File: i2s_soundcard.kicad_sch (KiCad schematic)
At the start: 19 parts, among them J1 Conn_01x08, J2 Conn_01x06, J3 Conn_01x04, J4 Conn_01x11, J5 Conn_01x03, U1 TLV320AIC3104IRHBT, U6 TLV7111830DSER, U7 TPD4E02B04DQAR, U8 TPD4E02B04DQAR

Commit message: Schematic: switch to AIC3206 to get ground-centered headphone outputs, and just wire up directly to a raspberry pi 40-pin header instead of using 1mm headers.
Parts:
- removed C2, C3: 220uF, Capacitor_SMD:C_1206_3216Metric, symbol Device:C
- removed C5: 22uF, Capacitor_SMD:C_0402_1005Metric, symbol Device:C
- removed C9: 220nF, Capacitor_SMD:C_0402_1005Metric, symbol Device:C
- removed J3: Conn_01x04, Connector_PinHeader_1.00mm:PinHeader_1x04_P1.00mm_Vertical, symbol Connector_Generic:Conn_01x04
- removed J4: Conn_01x11, Connector_PinHeader_1.00mm:PinHeader_1x11_P1.00mm_Vertical, symbol Connector_Generic:Conn_01x11
- removed U1: TLV320AIC3104IRHBT, footprints:TLV320AIC3104IRHBT, symbol TLV320AIC3104IRHBT:TLV320AIC3104IRHBT
- added C? (x2): 2.2uF, symbol Device:C
- added C? (x2): 10uF, Capacitor_SMD:C_0402_1005Metric, symbol Device:C
- added C?: 0.1uF, Capacitor_SMD:C_0402_1005Metric, symbol Device:C
- added C? (x2): 0.1u, symbol Device:C
- added C?: 1uF, symbol Device:C
- added J?: Conn_02x20_Odd_Even, symbol Connector_Generic:Conn_02x20_Odd_Even
- added R? (x2): 1k, symbol Device:R
- added U?: TLV320AIC3206IRSBR, RSB0040B, symbol TLV320AIC3206IRSBR:TLV320AIC3206IRSBR
- R1: value 2.2k -> 2.7k
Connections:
- net BCLK: now also J?.12 (Pin_12), U?.6 (BCLK)
- net DIN: now also J?.40 (Pin_40), U?.8 (DIN_MFP1)
- net DOUT: now also J?.38 (Pin_38), U?.9 (DOUT_MFP2)
- net GND: now also C?.1, C?.1, C?.1, C?.2, C?.2, J?.14 (Pin_14), J?.20 (Pin_20), J?.25 (Pin_25), J?.30 (Pin_30), J?.34 (Pin_34), J?.39 (Pin_39), J?.6 (Pin_6), J?.9 (Pin_9), R?.2, U?.1 (DVSS), U?.11 (IOVSS), U?.16 (SPI_SELECT), U?.2 (DVSS), U?.21 (AVSS), U?.37 (DVSS_CP), U?.41 (PAD); no longer J1.4 (Pin_4)
- net INTMIC_N: now also C?.2
- net INTMIC_P: now also C?.2
- net IOVDD: now also J?.1 (Pin_1), J?.17 (Pin_17), U?.10 (IOVDD)
- net LOL: now also U?.26 (LOL)
- net LOR: now also U?.27 (LOR)
- net MCLK: now also U?.5 (MCLK)
- net RING1: now also U?.33 (HPR)
- net SCL: now also J?.5 (Pin_5), U?.13 (SCL_SS_N)
- net SLEEVE: now also R1.2, U?.34 (MICDET); no longer R1.1
- net TIP: now also U?.31 (HPL)
- net VCC1.8: now also C?.2, C?.2, U?.29 (AVDD), U?.32 (DRVDD_HP), U?.39 (DVDD_CP), U?.40 (DVDD); no longer U6.6 (OUT1)
- net WCLK: now also J?.35 (Pin_35), U?.7 (WCLK)
- net at C1.1: now also U?.24 (IN3_L)
- net RING2: now reaches U7.5 (D2-)
- net RING2: now also J1.4 (Pin_4), U7.6 (NC), U?.28 (GND_SENSE)
- net EN1 renamed LDO_EN1
- net LDO_EN1: now also J?.15 (Pin_15)
- net EN2: no longer names the net of U6.3 (EN2)
- net VBAT_3.7 renamed VSYS
- net VSYS: now also C?.2, J?.2 (Pin_2), J?.4 (Pin_4), U?.30 (VSYS)
- net VCC3.0: no longer names the net of U6.5 (OUT2)
- new net: R1.1, R?.2, U?.23 (MICBIAS)
- new net: C?.1, U?.36 (FLY_N)
- new net: C?.2, U?.38 (FLY_P)
- new net: C?.1, R?.1, U?.18 (IN1_R)
- new net: C?.1, R?.1, U?.17 (IN1_L)
- new net: C?.1, U?.35 (VNEG)
- new net: C?.1, U?.22 (REF)
- new net CODEC_RESET: J?.13 (Pin_13), U?.3 (RESET_N)
- new net SDA: J?.3 (Pin_3), U?.14 (SDA_MOSI)
- new net ~AMP_SHUTDOWN: J?.11 (Pin_11)
- no-connect marks 4 -> 27
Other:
- sheet spkr_amp_left ports: added LINEIN; removed LINEIN+, LINEIN-
- sheet spkr_amp_right ports: added LINEIN; removed LINEIN+, LINEIN-
- moved on the sheet: C1, C10, C11, C4, C8, J1, R1, U7, U8

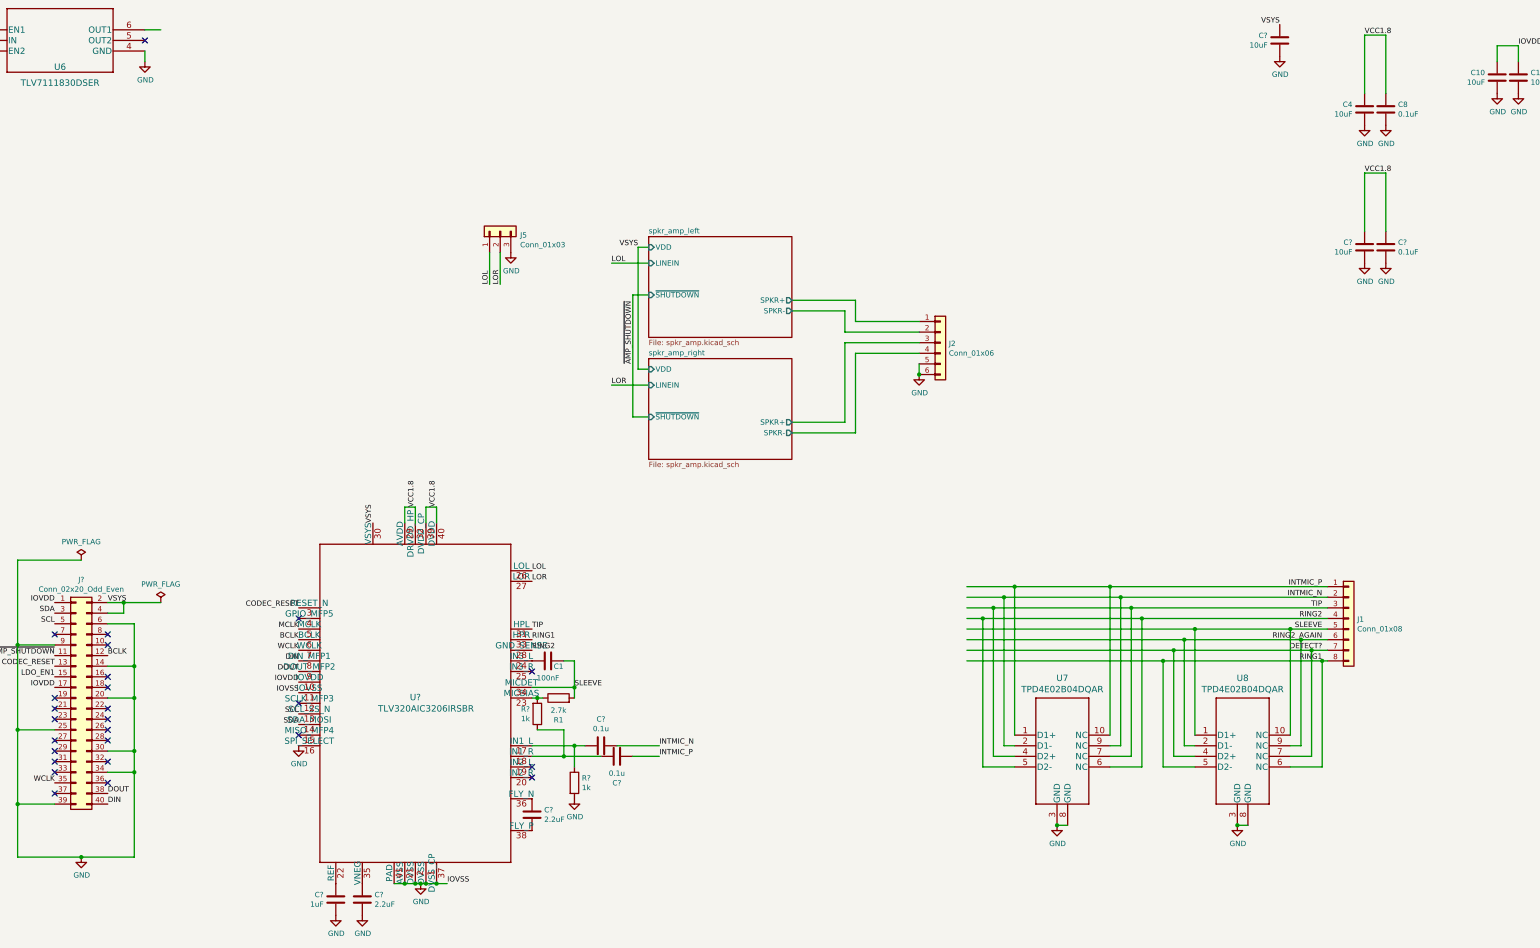
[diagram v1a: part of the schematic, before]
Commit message: lay out new version with AIC3206 codec
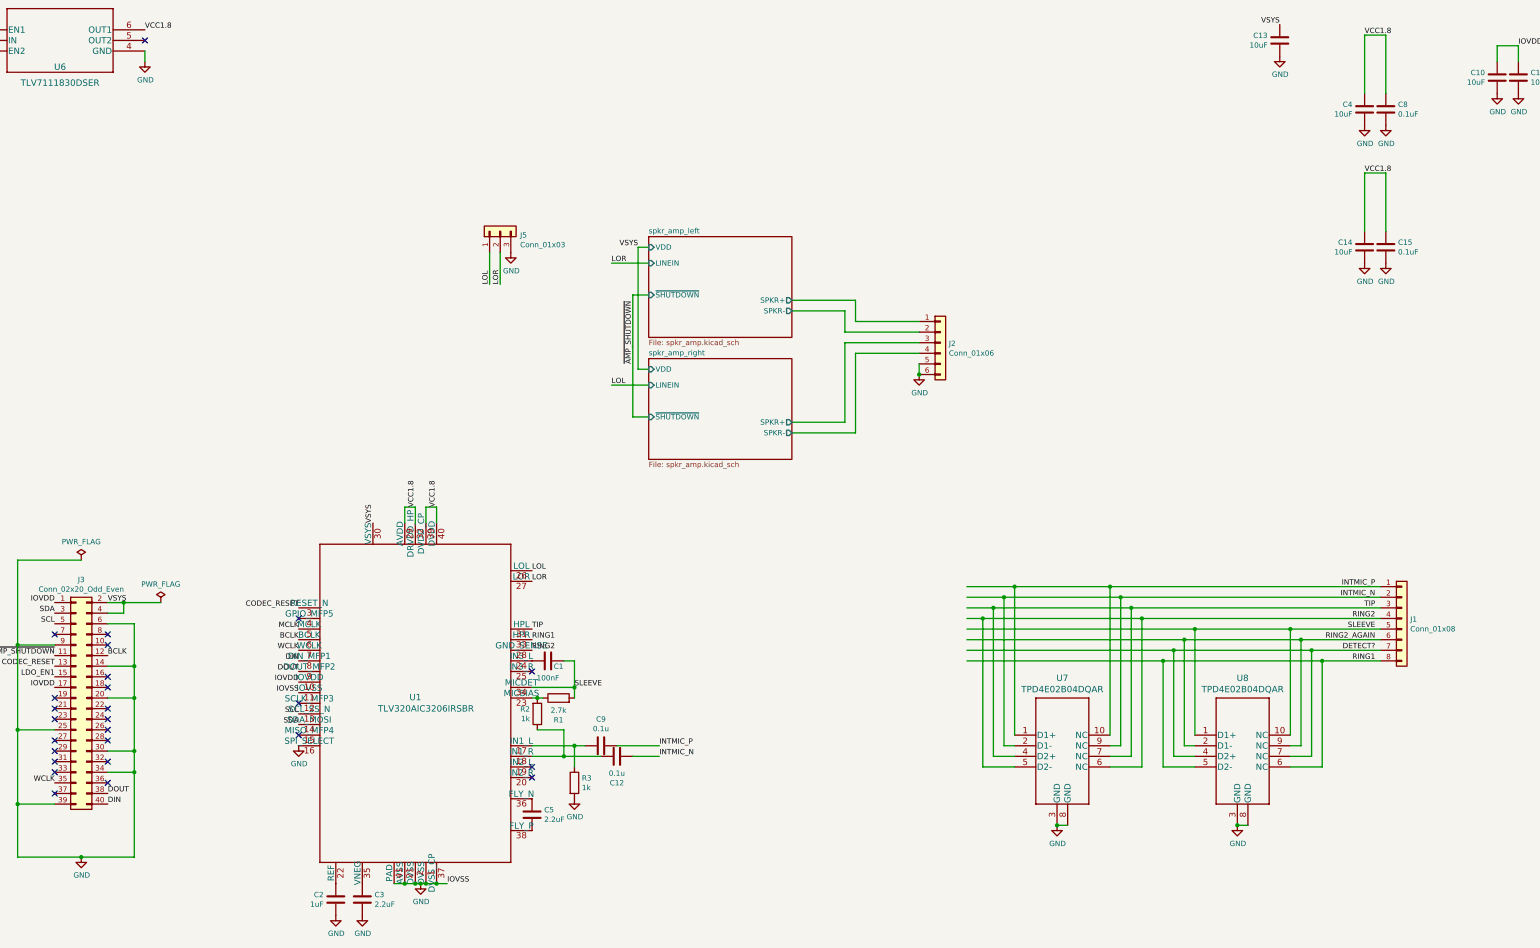
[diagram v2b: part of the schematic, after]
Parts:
- C12, C2, C3, C5, C9: renamed from C?; footprint (none) -> Capacitor_SMD:C_0402_1005Metric
- J3: renamed from J?; footprint (none) -> Connector_PinHeader_2.54mm:PinHeader_2x20_P2.54mm_Vertical
- J5: footprint Connector_PinHeader_1.00mm:PinHeader_1x03_P1.00mm_Vertical -> Connector_PinHeader_2.54mm:PinHeader_1x03_P2.54mm_Vertical
- R2, R3: renamed from R?; footprint (none) -> Resistor_SMD:R_0402_1005Metric
- U1: renamed from U?; footprint RSB0040B -> footprints:TLV320AIC3206IRSBR
- gave numbers to parts that had none: 3
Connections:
- net INTMIC_N: now also C12.2; no longer C9.2
- net INTMIC_P: now also C9.2; no longer C12.2
- net VCC1.8: now also U6.6 (OUT1)
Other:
- moved on the sheet: J1

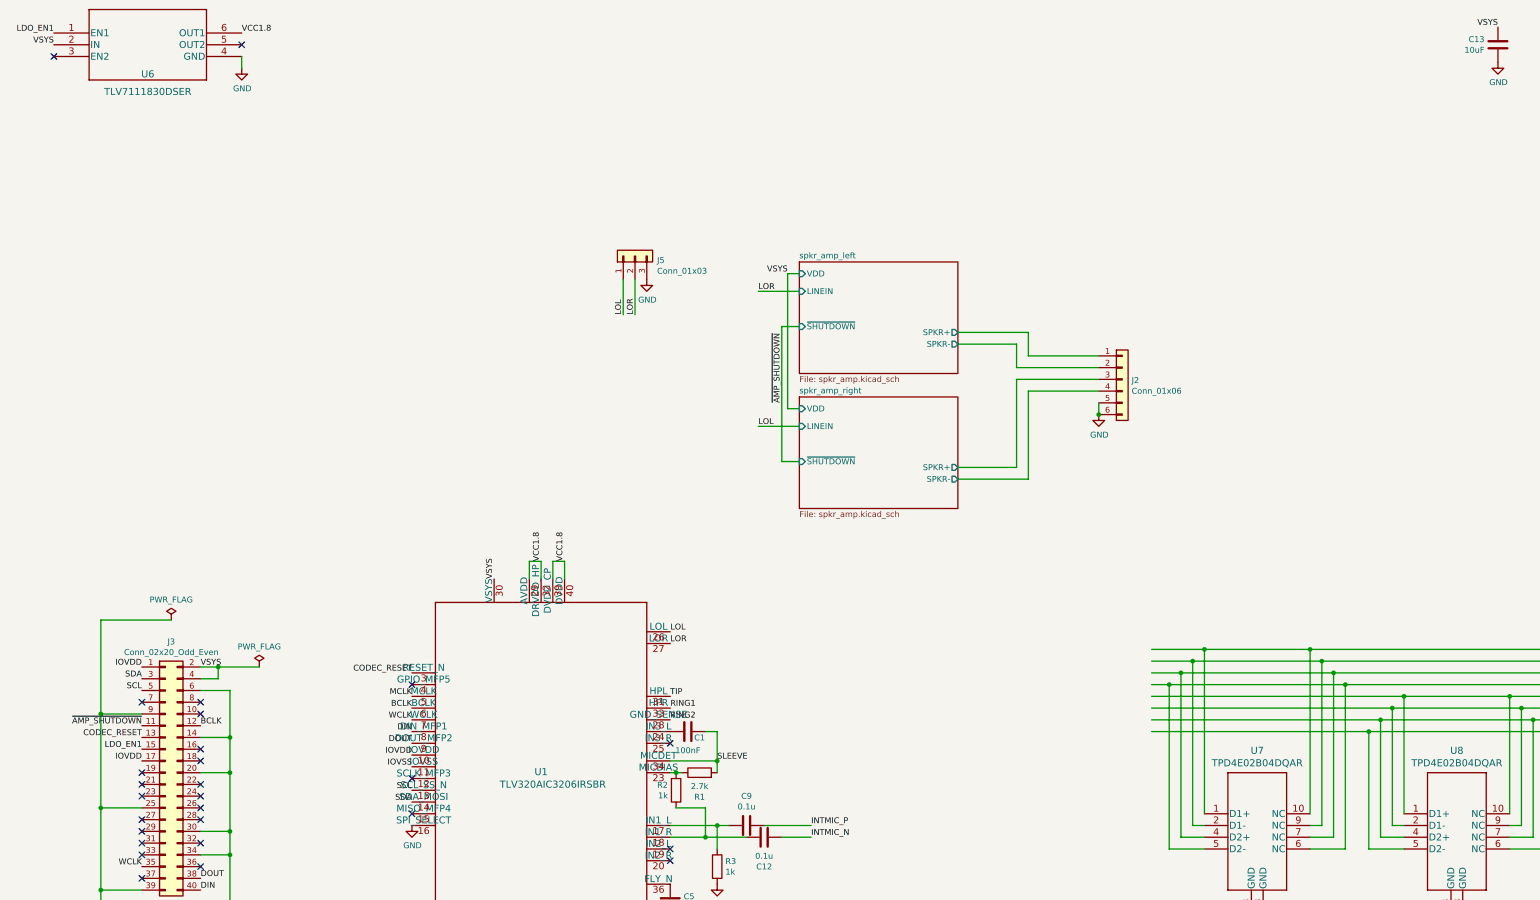
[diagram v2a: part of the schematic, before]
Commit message: Add an audio switch back in. Finish layout.
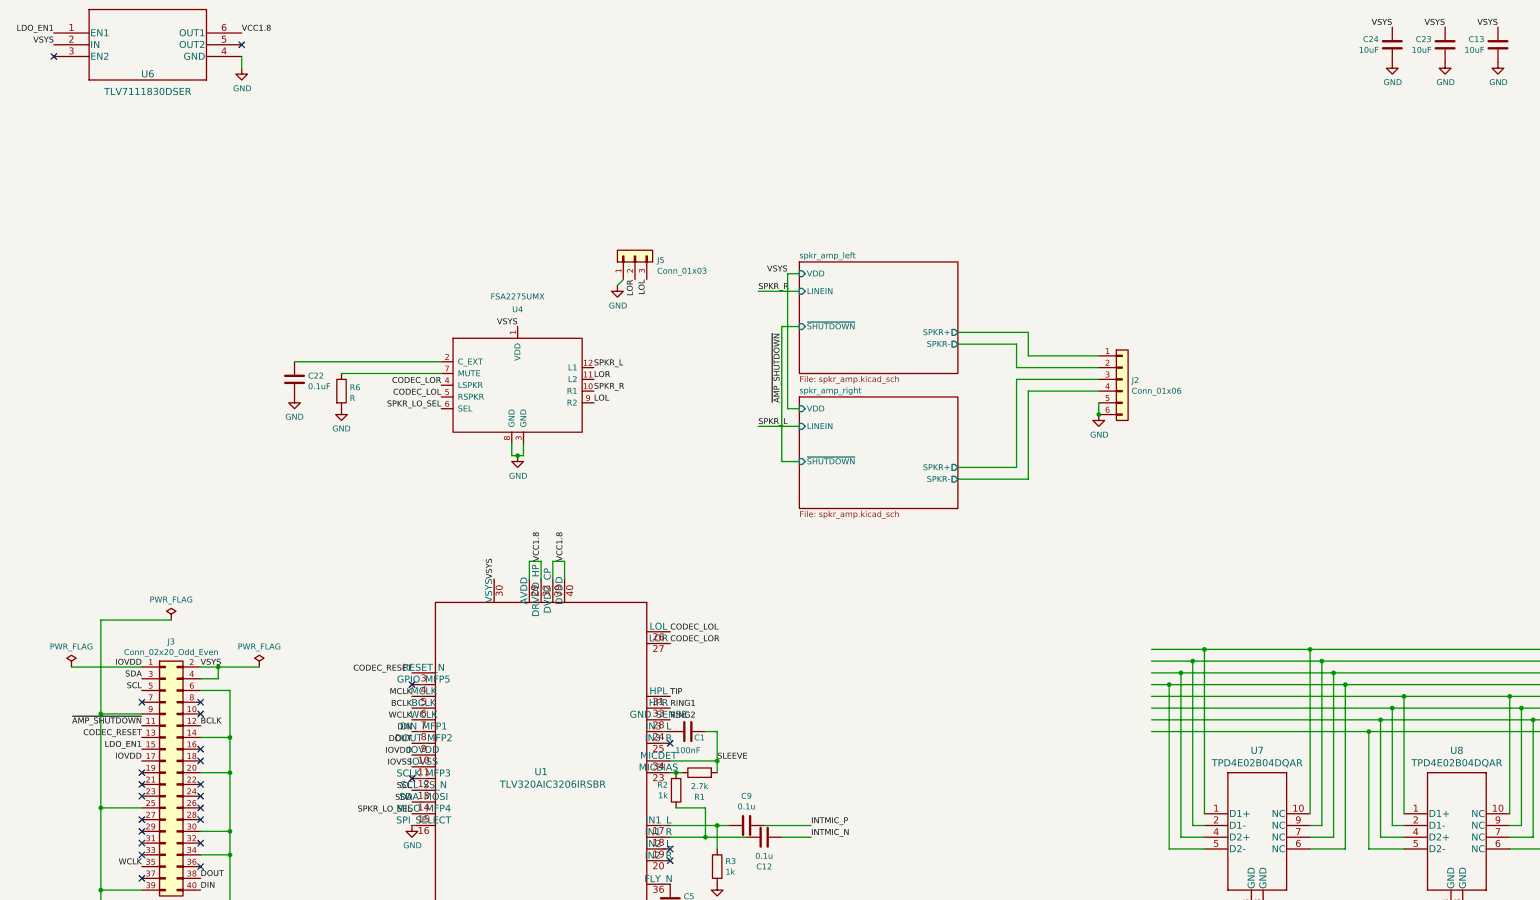
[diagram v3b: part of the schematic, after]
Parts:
- added C22: 0.1uF, Capacitor_SMD:C_0402_1005Metric, symbol Device:C
- added C23, C24: 10uF, Capacitor_SMD:C_0402_1005Metric, symbol Device:C
- added R6: R, Resistor_SMD:R_0402_1005Metric, symbol Device:R
- added U4: FSA2275UMX, footprints:FSA2275, symbol FSA2275UMX:FSA2275UMX
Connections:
- net GND: now also J5.1 (Pin_1), C22.2, C23.1, C24.1, R6.2, U4.3 (GND), U4.8 (GND); no longer J5.3 (Pin_3)
- net LOL: now also J5.3 (Pin_3), U4.9 (R2); no longer J5.1 (Pin_1), U1.26 (LOL)
- net LOR: now also U4.11 (L2); no longer U1.27 (LOR)
- net VSYS: now also C23.2, C24.2, U4.1 (VDD)
- net SPKR_LO_SEL: now reaches U1.15 (MISO_MFP4)
- net SPKR_LO_SEL: now also U4.6 (SEL)
- new net: C22.1, U4.2 (C_EXT)
- new net: R6.1, U4.7 (MUTE)
- new net CODEC_LOL: U1.26 (LOL), U4.5 (RSPKR)
- new net CODEC_LOR: U1.27 (LOR), U4.4 (LSPKR)
- new net SPKR_L: U4.12 (L1)
- new net SPKR_R: U4.10 (R1)
- no-connect marks 27 -> 26
